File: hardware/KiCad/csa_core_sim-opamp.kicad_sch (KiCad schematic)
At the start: 17 parts, among them Q1 MMDT3906, Q2 2SK932, U1 ${SIM.PARAMS}

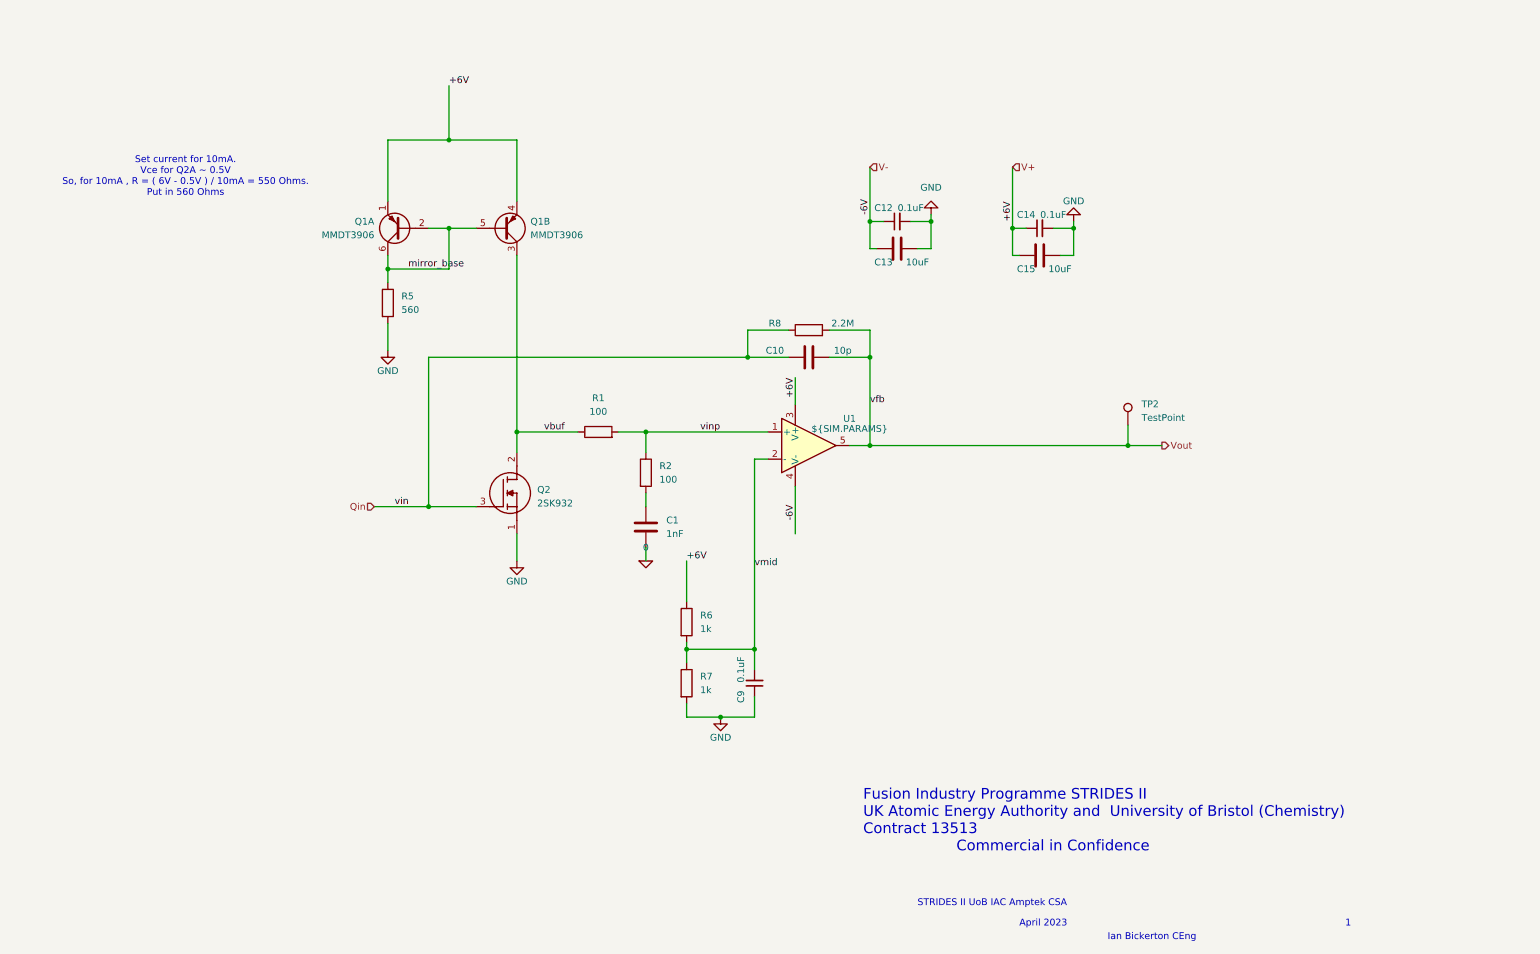
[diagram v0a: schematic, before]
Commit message: End of day save. Just needs voids added to planes to reduce capacitance
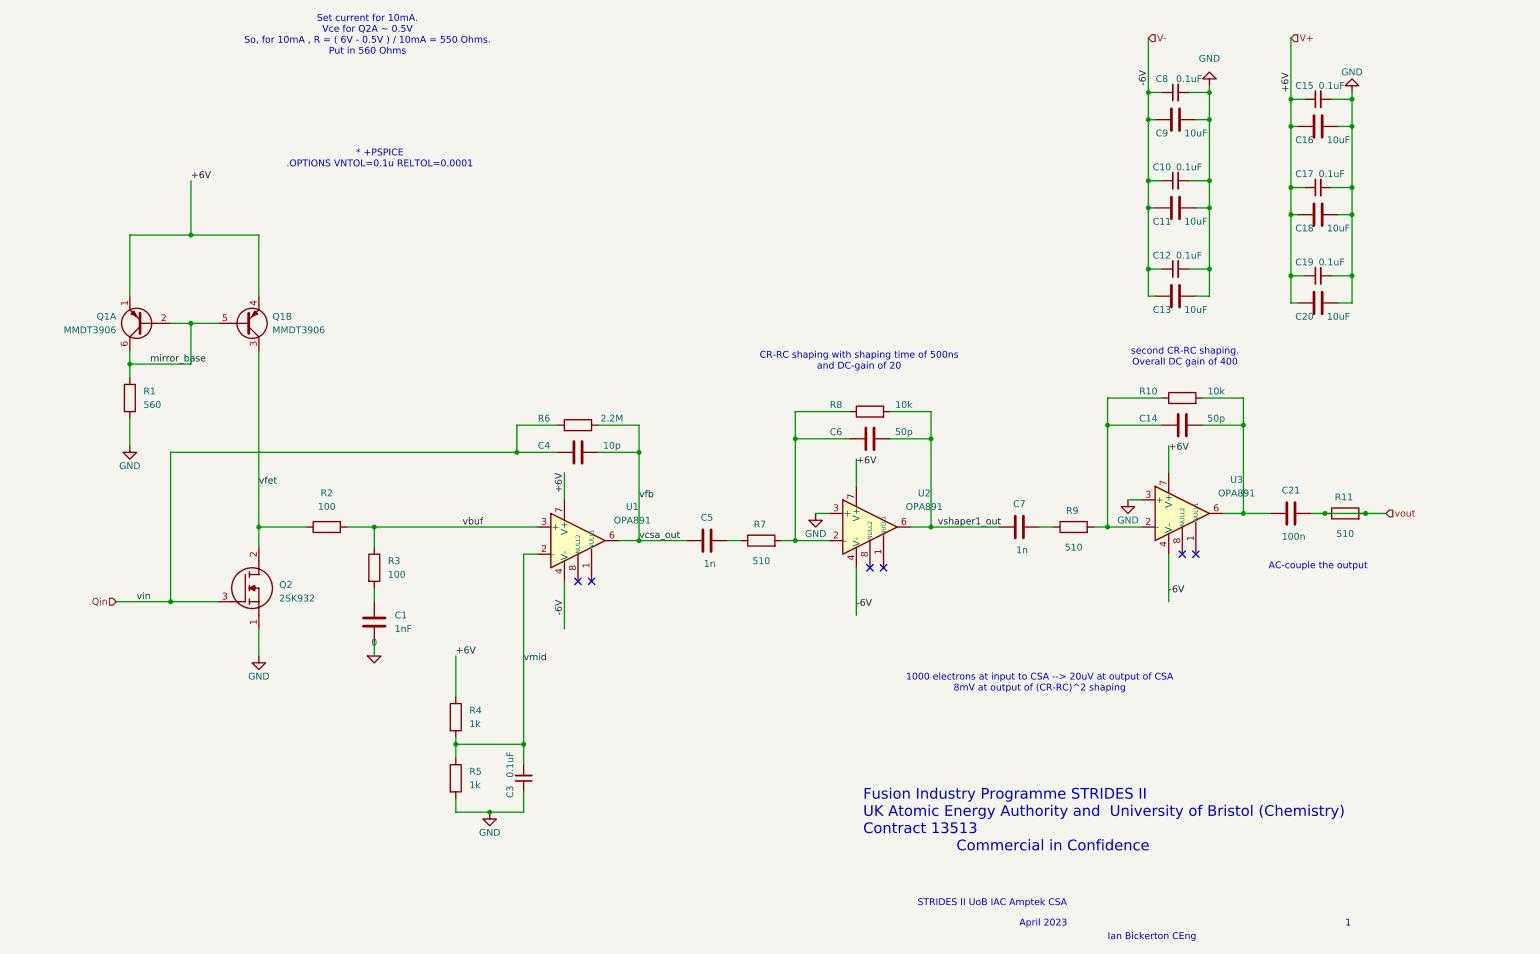
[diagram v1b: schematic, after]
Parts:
- removed C10: 10p, Resistor_SMD:R_0603_1608Metric_Pad0.98x0.95mm_HandSolder, symbol Device:C
- removed C14, C9: 0.1uF, Capacitor_SMD:C_0805_2012Metric, symbol Device:C_Small
- removed C15: 10uF, Capacitor_SMD:C_0805_2012Metric, symbol Device:C
- removed TP2: TestPoint, TestPoint:TestPoint_Pad_2.0x2.0mm, symbol Connector:TestPoint
- removed U1: ${SIM.PARAMS}, symbol Simulation_SPICE:OPAMP
- added C10, C15, C17, C19, C3, C8: 0.1uF, Capacitor_SMD:C_0805_2012Metric, symbol Device:C_Small
- added C11, C16, C18, C20, C9: 10uF, Capacitor_SMD:C_0805_2012Metric, symbol Device:C
- added C14, C6: 50p, Resistor_SMD:R_0603_1608Metric_Pad0.98x0.95mm_HandSolder, symbol Device:C
- added C21: 100n, Resistor_SMD:R_0603_1608Metric_Pad0.98x0.95mm_HandSolder, symbol Device:C
- added C4: 10p, Resistor_SMD:R_0603_1608Metric_Pad0.98x0.95mm_HandSolder, symbol Device:C
- added C5, C7: 1n, Resistor_SMD:R_0603_1608Metric_Pad0.98x0.95mm_HandSolder, symbol Device:C
- added R10: 10k, Resistor_SMD:R_0603_1608Metric_Pad0.98x0.95mm_HandSolder, symbol Device:R
- added R11, R9: 510, Resistor_SMD:R_0603_1608Metric_Pad0.98x0.95mm_HandSolder, symbol Device:R
- added R3: 100, symbol Device:R
- added R4: 1k, Resistor_SMD:R_0603_1608Metric, symbol Device:R
- added U1, U2, U3: OPA891, Package_SO:SOIC-8_7.5x5.85mm_P1.27mm, symbol OPA891:OPA891
- R1: value 100 -> 560; footprint (none) -> Resistor_SMD:R_0603_1608Metric
- R5: value 560 -> 1k
- R6: value 1k -> 2.2M; footprint Resistor_SMD:R_0603_1608Metric -> Resistor_SMD:R_0603_1608Metric_Pad0.98x0.95mm_HandSolder
- R7: value 1k -> 510; footprint Resistor_SMD:R_0603_1608Metric -> Resistor_SMD:R_0603_1608Metric_Pad0.98x0.95mm_HandSolder
- R8: value 2.2M -> 10k
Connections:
- net GND: now also R1.2, C10.2, C11.2, C15.2, C16.2, C17.2, C18.2, C19.2, C20.2, C3.1, C8.2, C9.2, U2.3 (+), U3.3 (+); no longer R7.2
- net Qin: now also R6.1, C4.1; no longer R8.1
- net V+: now also C15.1, C16.1, C17.1, C18.1, C19.1, C20.1, R4.1, U1.7 (V+), U2.7 (V+), U3.7 (V+); no longer R6.1
- net V-: now also C10.1, C11.1, C8.1, C9.1, U1.4 (V-), U2.4 (V-), U3.4 (V-)
- net mirror_base: now also R1.1; no longer R5.1
- net vbuf: now also R2.2, R3.1, U1.3 (+); no longer Q1.3 (C2), Q2.2 (D), R1.1
- net vmid: now also R5.1, C3.2, R4.2, U1.2 (-); no longer R6.2, R7.1
- net at C1.1: now also R3.2; no longer R2.2
- net Vout renamed vshaper1_out
- net vshaper1_out: now also C6.2, C7.1, U2.6
- net vinp renamed vfet
- net vfet: now also Q1.3 (C2), Q2.2 (D); no longer R1.2
- new net: C7.2, R9.1
- new net: C14.1, R10.1, R9.2, U3.2 (-)
- new net: C14.2, C21.1, R10.2, U3.6
- new net: C6.1, R7.2, R8.1, U2.2 (-)
- new net: C5.2, R7.1
- new net vcsa_out: C4.2, C5.1, R6.2, U1.6
- new net vout: C21.2, R11.1, R11.2
- no-connect marks 0 -> 6
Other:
- note added: "* +PSPICE .OPTIONS VNTOL=0.1u RELTOL=0.0001"
- note added: "1000 electrons at input to CSA --> 20uV at output of CSA 8mV at output of (CR-RC)^2 shaping"
- note added: "AC-couple the output"
- note added: "CR-RC shaping with shaping time of 500ns and DC-gain of 20"
- note added: "second CR-RC shaping. Overall DC gain of 400"
